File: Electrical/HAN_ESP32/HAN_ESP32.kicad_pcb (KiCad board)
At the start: 2 copper layers, 80 x 33.1 mm, 34 parts, among them J1 8P8C_Shielded, J2 USB_B_Micro, J3 Conn_01x06, Q1 BSS84, SW1 ESP_RESET, SW2 ESP_PROG, U1 AP7375-33SA, U2 ESP32-WROOM-32, U3 TSS721

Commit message: Initial layout done
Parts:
- moved R2 48.4 mm to (108.7, 112.7), turned to 180 degrees
- moved R1 41.2 mm to (108.7, 110.3), turned to 180 degrees
- moved C4 34.7 mm to (171.0, 118.3), turned to 180 degrees
- moved R6 32.7 mm to (108.5, 116.3)
- moved JP2 29.3 mm to (130.3, 126.2), turned to 0 degrees
- moved JP1 28.3 mm to (130.3, 119.6), turned to 0 degrees
- moved C5 27.5 mm to (116.2, 131.3)
- moved R8 26.2 mm to (125.4, 121.1), turned to -90 degrees
- moved R3 21.6 mm to (103.3, 110.3), turned to 180 degrees
- moved R5 21.2 mm to (101.8, 114.1), turned to -90 degrees
- moved R4 21.1 mm to (104.7, 114.1), turned to -90 degrees
- moved R10 20.3 mm to (153.6, 129.0)
- moved Q1 19.9 mm to (126.4, 129.0)
- moved C3 19.7 mm to (111.2, 121.7), turned to 180 degrees
- moved C8 18.3 mm to (136.6, 115.3)
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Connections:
- J1 pad SH: unconnected-(J1-PadSH) -> GND
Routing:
- net VDD: track 0.00 -> 64.9 mm, vias 0 -> 2
- net +3V3: track 0.00 -> 58.2 mm, vias 0 -> 1
- net /ESP_TX: track 0.00 -> 44.5 mm, vias 0 -> 1
- net /ESP_RX: track 0.00 -> 44.2 mm, vias 0 -> 1
- net Net-(C8-Pad2): track 0.00 -> 34.4 mm, vias 0 -> 2
- net /HAN_TX: track 0.00 -> 25.2 mm
- net Net-(R5-Pad2): track 0.00 -> 23.5 mm
- net Net-(C9-Pad1): track 0.00 -> 20.6 mm
- net /HAN_RX: track 0.00 -> 9.88 mm
- net Net-(J1-Pad2): track 0.00 -> 9.63 mm
- net Net-(R6-Pad2): track 0.00 -> 8.81 mm
- net Net-(J1-Pad1): track 0.00 -> 8.74 mm
- net Net-(C1-Pad1): track 0.00 -> 6.55 mm
- net Net-(C5-Pad1): track 0.00 -> 6.35 mm
- net Net-(C3-Pad1): track 0.00 -> 6.14 mm
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- added copper zone on B.Cu, net GND
- added copper zone on F.Cu, net GND
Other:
- board text added: "GND"
- board text added: "HAN Sensor"
- board text added: "JP RX"
- board text added: "JP TX"
- board text added: "PROG"
- board text added: "RST"
- board text added: "RX"
- board text added: "TX"

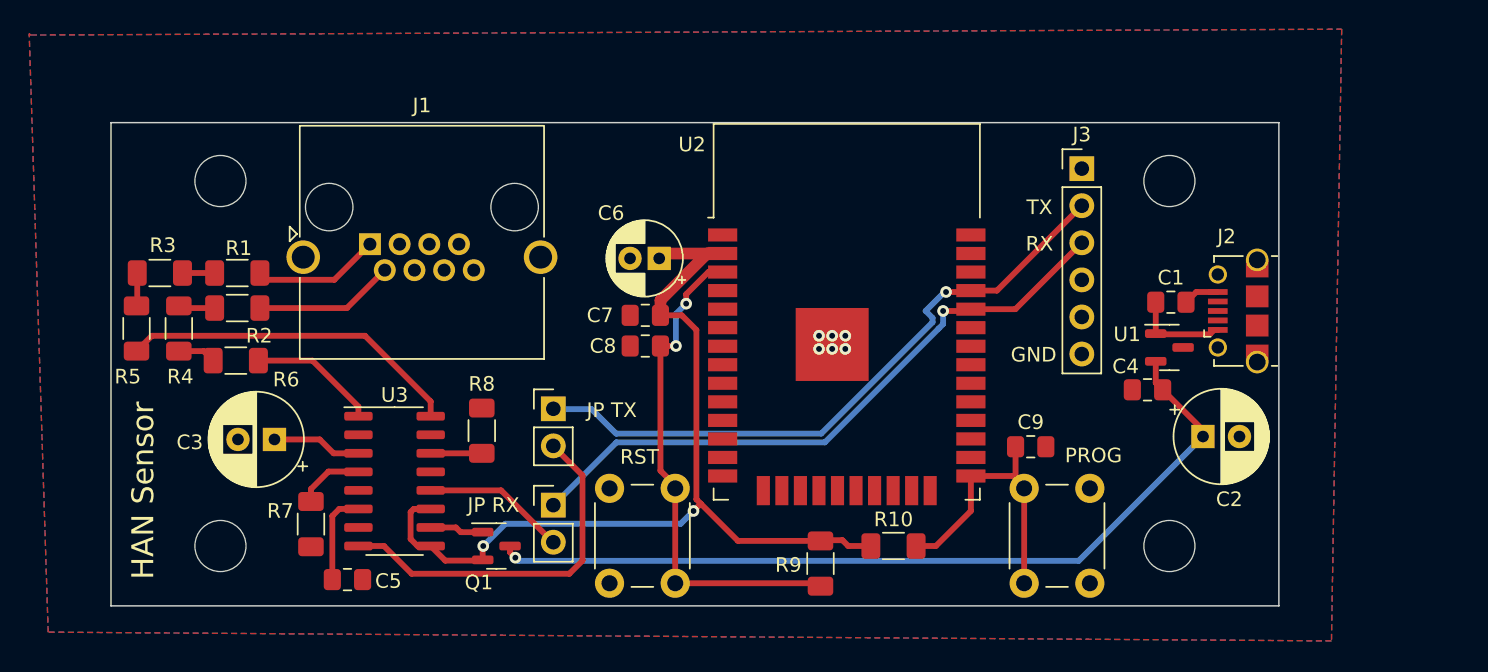
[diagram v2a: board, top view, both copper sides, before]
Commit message: Changed PCB shape to have connectors on tha wall of the enclosure
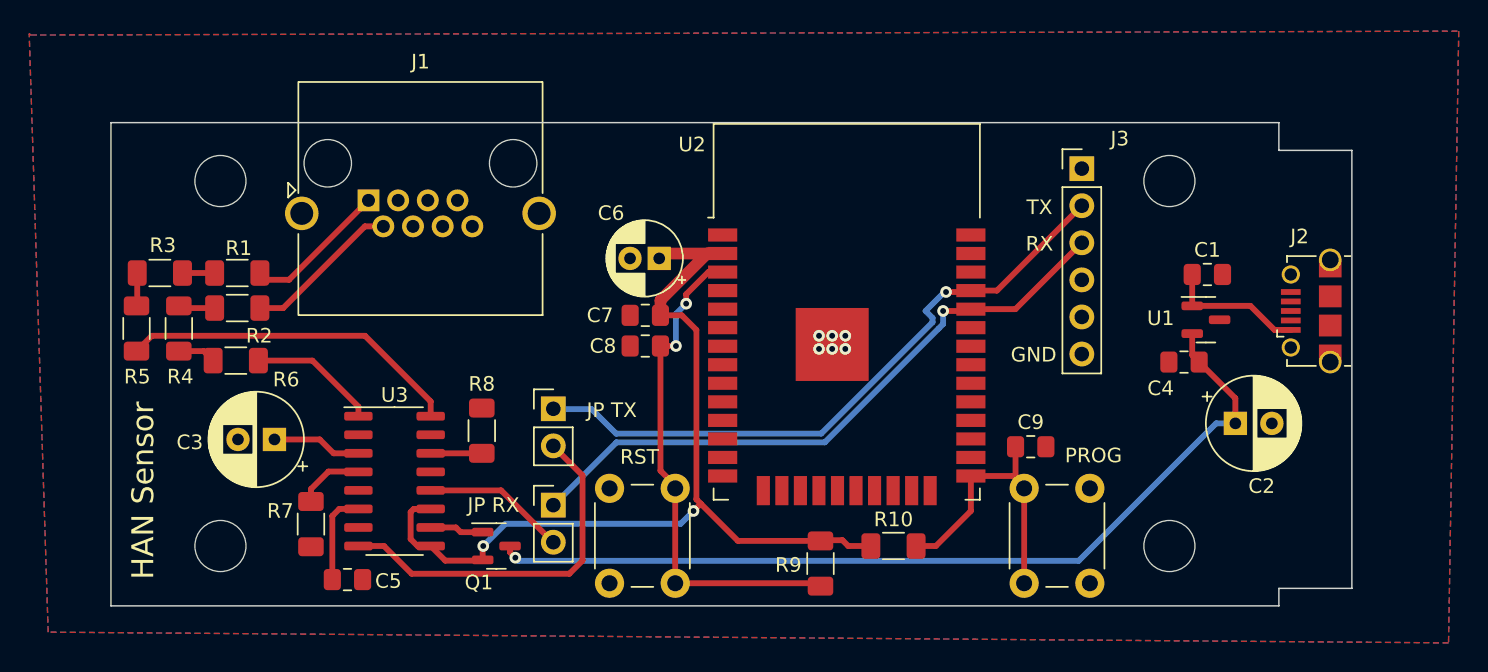
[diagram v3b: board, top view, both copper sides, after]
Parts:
- moved J2 5.00 mm to (182.2, 112.9)
- moved U1 3.14 mm to (175.0, 113.5)
- moved C1 3.14 mm to (175.1, 110.4)
- moved C4 3.14 mm to (173.5, 116.4)
- moved J1 3.00 mm to (117.6, 105.3)
- moved C2 2.39 mm to (177.0, 120.6)
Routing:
- net +3V3: track 58.2 -> 61.6 mm
- net Net-(C1-Pad1): track 6.55 -> 9.59 mm
- net GND: track 2.47 -> 0.00 mm
- net Net-(J1-Pad2): track 9.63 -> 10.8 mm
- net Net-(J1-Pad1): track 8.74 -> 9.89 mm
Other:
- board size 80 x 33.1 mm -> 85 x 33.1 mm
